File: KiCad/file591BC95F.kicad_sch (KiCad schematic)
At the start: 51 parts, among them J203 V4, P201 Power Pole, P203 Power Pole, Q201 MUN5213DW1, Q202 DMP4025LSD, Q203 RJK0354DSP, U202 OPA171, U203 LTC3600, U204 MIC2196

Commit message: KiCad Updates
o Fixes for problems found during first board build
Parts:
- P201: footprint Oddities:Dummy_Empty_2 -> Connect:PowerPole-ASMPP30-1x2; Manufacturer TH -> Anderson Power Products, Inc.
- P203: Manufacturer TH -> Anderson Power Products, Inc.
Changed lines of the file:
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@@
       (effects (font (size 1.524 1.524)) hide)
     )
-    (property "Manufacturer" "TH" (id 6) (at 152.4 129.54 0)
+    (property "Manufacturer" "Anderson Power Products, Inc." (id 6) (at 152.4 129.54 0)
       (effects (font (size 1.27 1.27)) hide)
     )
@@
     (property "Reference" "P201" (id 0) (at 160.02 124.46 0))
     (property "Value" "Power Pole" (id 1) (at 156.21 128.27 90))
-    (property "Footprint" "Oddities:Dummy_Empty_2" (id 2) (at 160.02 128.27 0)
+    (property "Footprint" "Connect:PowerPole-ASMPP30-1x2" (id 2) (at 160.02 128.27 0)
       (effects (font (size 1.27 1.27)) hide)
     )
@@
       (effects (font (size 1.524 1.524)) hide)
     )
-    (property "Manufacturer" "TH" (id 6) (at 160.02 128.27 0)
+    (property "Manufacturer" "Anderson Power Products, Inc." (id 6) (at 160.02 128.27 0)
       (effects (font (size 1.27 1.27)) hide)
     )
@@
       (effects (font (size 1.27 1.27)) hide)
     )
-    (property "Description" "TH" (id 8) (at 160.02 128.27 0)
-      (effects (font (size 1.27 1.27)) hide)
-    )
+    (property "Value" "Power Pole" (id 8) (at 160.02 128.27 0)
+      (effects (font (size 1.27 1.27)) hide)
+    )
+    (property "Footprint" "Connect:PowerPole-ASMPP30-1x2" (id 9) (at 160.02 128.27 0)
+      (effects (font (size 1.27 1.27)) hide)
+    )

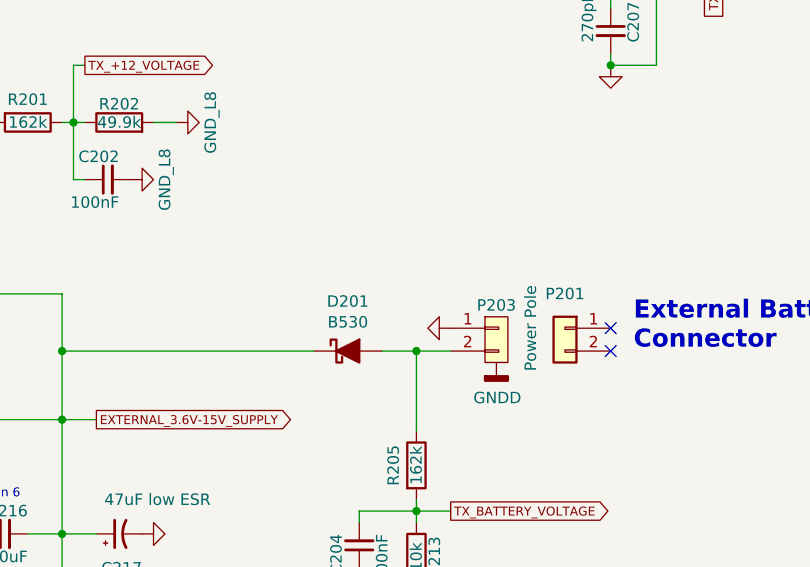
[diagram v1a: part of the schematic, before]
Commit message: Updates
Schematic
Fixes to events.html
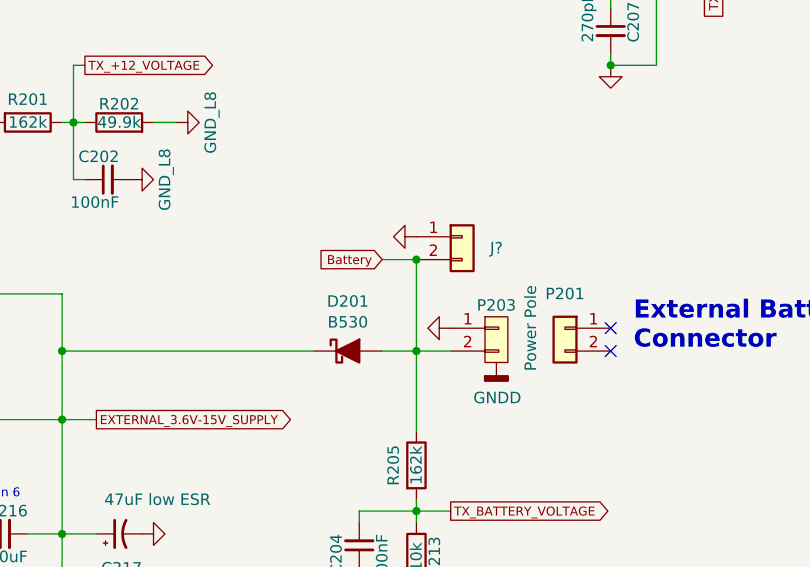
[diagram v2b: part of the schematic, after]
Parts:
- added J?: (no value), symbol Connector_Generic:Conn_01x02
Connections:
- net GND: now also J?.1 (Pin_1)
- net Battery: now reaches D201.2 (A), P203.2 (P2), R205.1
- net Battery: now also J?.2 (Pin_2)
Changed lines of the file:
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@@
   (junction (at 143.51 148.59) (diameter 0) (color 0 0 0 0)
+  )
+  (junction (at 143.51 120.65) (diameter 0) (color 0 0 0 0)
   )
   (junction (at 54.61 165.1) (diameter 0) (color 0 0 0 0)
@@
     (stroke (width 0) (type default) (color 0 0 0 0))
   )
+  (wire (pts (xy 143.51 120.65) (xy 143.51 130.81))
+    (stroke (width 0) (type default) (color 0 0 0 0))
+  )
   (wire (pts (xy 80.01 162.56) (xy 80.01 157.48))
     (stroke (width 0) (type default) (color 0 0 0 0))
@@
   )
   (wire (pts (xy 49.53 105.41) (xy 63.5 105.41))
+    (stroke (width 0) (type default) (color 0 0 0 0))
+  )
+  (wire (pts (xy 139.7 120.65) (xy 143.51 120.65))
     (stroke (width 0) (type default) (color 0 0 0 0))
   )
@@
     (property "Intersheet References" "${INTERSHEET_REFS}" (id 0) (at 0 0 0)
       (effects (font (size 1.27 1.27)) hide)
+    )
+  )
+  (global_label "Battery" (shape input) (at 139.7 120.65 180) (fields_autoplaced)
+    (effects (font (size 0.9906 0.9906)) (justify right))
+    (property "Intersheet References" "${INTERSHEET_REFS}" (id 0) (at 132.6513 120.5881 0)
+      (effects (font (size 0.9906 0.9906)) (justify right) hide)
     )
   )
@@
     (pin "2")
   )
+  (symbol (lib_id "Connector_Generic:Conn_01x02") (at 148.59 118.11 0) (unit 1)
+    (in_bom yes) (on_board yes)
+    (property "Reference" "J?" (id 0) (at 152.4 119.38 0))
+    (property "Value" "" (id 1) (at 146.5072 124.0536 0)
+      (effects (font (size 1.27 1.27)) hide)
+    )
+    (property "Footprint" "" (id 2) (at 148.59 118.11 0)
+      (effects (font (size 1.27 1.27)) hide)
+    )
+    (property "Datasheet" "~" (id 3) (at 148.59 118.11 0)
+      (effects (font (size 1.27 1.27)) hide)
+    )
+    (pin "1")
+    (pin "2")
+  )
+  (symbol (lib_id "FlexFox80-rescue:GND_L8-ARDF-2-Band-MiniTx-rescue") (at 143.51 118.11 270) (unit 1)
+    (in_bom yes) (on_board yes)
+    (property "Reference" "#PWR?" (id 0) (at 137.16 118.11 0)
+      (effects (font (size 1.27 1.27)) hide)
+    )
+    (property "Value" "GND_L8" (id 1) (at 139.7 118.11 0)
+      (effects (font (size 1.27 1.27)) hide)
+    )
+    (property "Footprint" "" (id 2) (at 143.51 118.11 0))
+    (property "Datasheet" "" (id 3) (at 143.51 118.11 0))
+    (pin "1")
+  )
 )
